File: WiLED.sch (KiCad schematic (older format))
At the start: 23 parts, among them P1 DC In, P2 LED Connector, P3 Serial to USB, P4 ADAFRUIT_FEATHER, SW1 Reset, SW2 Bootload, U1 ESP-12, U2 R-78E-0.5

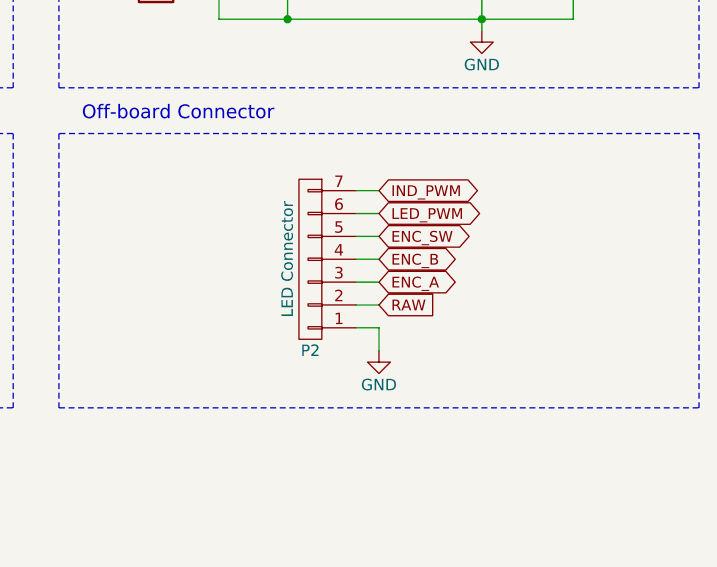
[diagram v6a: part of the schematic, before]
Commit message: Add pull-down on LED_PWM. Closes #1
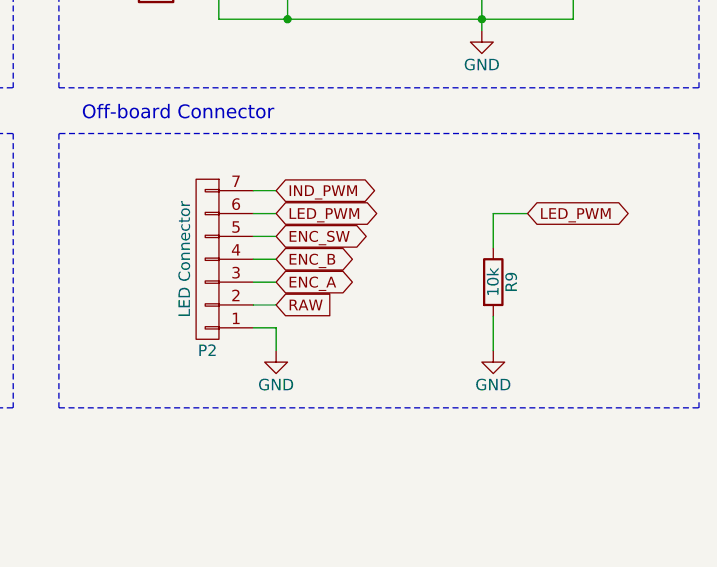
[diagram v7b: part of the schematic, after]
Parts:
- added R9: 10k, Resistors_SMD:R_0805_HandSoldering, symbol R
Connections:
- net GND: now also R9.2
- net LED_PWM: now also R9.1
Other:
- moved on the sheet: P2
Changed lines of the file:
@@
 Sheet 1 1
 Title "WiLED ESP-12 Feather"
-Date "2017-09-10"
-Rev "1.0"
+Date "2017-09-25"
+Rev "1.1"
 Comp "Sean Lanigan"
 Comment1 "Requires RF69 Featherwing to connect to low-power radio network."
@@
 $EndComp
 $Comp
-L GND #PWR01
+L GND #PWR1
 U 1 1 5988430F
 P 2050 1350
-F 0 "#PWR01" H 2050 1100 50  0001 C CNN
+F 0 "#PWR1" H 2050 1100 50  0001 C CNN
 F 1 "GND" H 2050 1200 50  0000 C CNN
 F 2 "" H 2050 1350 50  0000 C CNN
@@
 $EndComp
 $Comp
-L +3.3V #PWR02
+L +3.3V #PWR2
 U 1 1 598859CA
 P 2450 4150
-F 0 "#PWR02" H 2450 4000 50  0001 C CNN
+F 0 "#PWR2" H 2450 4000 50  0001 C CNN
 F 1 "+3.3V" H 2450 4290 50  0000 C CNN
 F 2 "" H 2450 4150 50  0000 C CNN
@@
 $EndComp
 $Comp
-L GND #PWR03
+L GND #PWR3
 U 1 1 59885B82
 P 2450 4900
-F 0 "#PWR03" H 2450 4650 50  0001 C CNN
+F 0 "#PWR3" H 2450 4650 50  0001 C CNN
 F 1 "GND" H 2450 4750 50  0000 C CNN
 F 2 "" H 2450 4900 50  0000 C CNN
@@
 RST
 $Comp
-L +3.3V #PWR04
+L +3.3V #PWR14
 U 1 1 599572FE
 P 8550 1150
-F 0 "#PWR04" H 8550 1000 50  0001 C CNN
+F 0 "#PWR14" H 8550 1000 50  0001 C CNN
 F 1 "+3.3V" H 8550 1290 50  0000 C CNN
 F 2 "" H 8550 1150 50  0000 C CNN
@@
 $EndComp
 $Comp
-L GND #PWR05
+L GND #PWR15
 U 1 1 599575DC
 P 8550 1850
-F 0 "#PWR05" H 8550 1600 50  0001 C CNN
+F 0 "#PWR15" H 8550 1600 50  0001 C CNN
 F 1 "GND" H 8550 1700 50  0000 C CNN
 F 2 "" H 8550 1850 50  0000 C CNN
@@
 EN
 $Comp
-L +3.3V #PWR06
+L +3.3V #PWR16
 U 1 1 59957B8D
 P 9100 1150
-F 0 "#PWR06" H 9100 1000 50  0001 C CNN
+F 0 "#PWR16" H 9100 1000 50  0001 C CNN
 F 1 "+3.3V" H 9100 1290 50  0000 C CNN
 F 2 "" H 9100 1150 50  0000 C CNN
@@
 $EndComp
 $Comp
-L +3.3V #PWR07
+L +3.3V #PWR4
 U 1 1 599586BB
 P 2650 1250
-F 0 "#PWR07" H 2650 1100 50  0001 C CNN
+F 0 "#PWR4" H 2650 1100 50  0001 C CNN
 F 1 "+3.3V" H 2650 1390 50  0000 C CNN
 F 2 "" H 2650 1250 50  0000 C CNN
@@
 LED_PWM
 $Comp
-L GND #PWR08
+L GND #PWR5
 U 1 1 59959BA4
 P 2650 3200
-F 0 "#PWR08" H 2650 2950 50  0001 C CNN
+F 0 "#PWR5" H 2650 2950 50  0001 C CNN
 F 1 "GND" H 2650 3050 50  0000 C CNN
 F 2 "" H 2650 3200 50  0000 C CNN
@@
 2
 $Comp
-L +3.3V #PWR09
+L +3.3V #PWR18
 U 1 1 5995A16C
 P 9650 1150
-F 0 "#PWR09" H 9650 1000 50  0001 C CNN
+F 0 "#PWR18" H 9650 1000 50  0001 C CNN
 F 1 "+3.3V" H 9650 1290 50  0000 C CNN
 F 2 "" H 9650 1150 50  0000 C CNN
@@
 0
 $Comp
-L +3.3V #PWR010
+L +3.3V #PWR21
 U 1 1 5995A6E0
 P 10200 1150
-F 0 "#PWR010" H 10200 1000 50  0001 C CNN
+F 0 "#PWR21" H 10200 1000 50  0001 C CNN
 F 1 "+3.3V" H 10200 1290 50  0000 C CNN
 F 2 "" H 10200 1150 50  0000 C CNN
@@
 $EndComp
 $Comp
-L GND #PWR011
+L GND #PWR22
 U 1 1 5995ABD4
 P 10200 1850
-F 0 "#PWR011" H 10200 1600 50  0001 C CNN
+F 0 "#PWR22" H 10200 1600 50  0001 C CNN
 F 1 "GND" H 10200 1700 50  0000 C CNN
 F 2 "" H 10200 1850 50  0000 C CNN
@@
 15
 $Comp
-L GND #PWR012
+L GND #PWR24
 U 1 1 5995B592
 P 10750 1850
-F 0 "#PWR012" H 10750 1600 50  0001 C CNN
+F 0 "#PWR24" H 10750 1600 50  0001 C CNN
 F 1 "GND" H 10750 1700 50  0000 C CNN
 F 2 "" H 10750 1850 50  0000 C CNN
@@
 $EndComp
 $Comp
-L GND #PWR013
+L GND #PWR19
 U 1 1 5996B043
 P 10000 3250
-F 0 "#PWR013" H 10000 3000 50  0001 C CNN
+F 0 "#PWR19" H 10000 3000 50  0001 C CNN
 F 1 "GND" H 10000 3100 50  0000 C CNN
 F 2 "" H 10000 3250 50  0000 C CNN
@@
 $EndComp
 $Comp
-L +3.3V #PWR014
+L +3.3V #PWR23
 U 1 1 5996BEF5
 P 10500 2600
-F 0 "#PWR014" H 10500 2450 50  0001 C CNN
+F 0 "#PWR23" H 10500 2450 50  0001 C CNN
 F 1 "+3.3V" H 10500 2740 50  0000 C CNN
 F 2 "" H 10500 2600 50  0000 C CNN
@@
 Text GLabel 3550 4700 0    47   Input ~ 0
 RAW
-Text GLabel 9550 4450 2    47   Input ~ 0
+Text GLabel 9100 4450 2    47   Input ~ 0
 RAW
 $Comp
-L GND #PWR015
+L GND #PWR17
 U 1 1 5997B5E9
-P 9550 4650
-F 0 "#PWR015" H 9550 4400 50  0001 C CNN
-F 1 "GND" H 9550 4500 50  0000 C CNN
-F 2 "" H 9550 4650 50  0000 C CNN
-F 3 "" H 9550 4650 50  0000 C CNN
-	1    9550 4650
-	1    0    0    -1
-$EndComp
-Text GLabel 9550 4050 2    47   BiDi ~ 0
+P 9100 4650
+F 0 "#PWR17" H 9100 4400 50  0001 C CNN
+F 1 "GND" H 9100 4500 50  0000 C CNN
+F 2 "" H 9100 4650 50  0000 C CNN
+F 3 "" H 9100 4650 50  0000 C CNN
+	1    9100 4650
+	1    0    0    -1
+$EndComp
+Text GLabel 9100 4050 2    47   BiDi ~ 0
 LED_PWM
 Text GLabel 3800 2350 2    47   BiDi ~ 0
@@
 Text GLabel 3800 2550 2    47   BiDi ~ 0
 ENC_B
-Text GLabel 9550 4350 2    47   BiDi ~ 0
+Text GLabel 9100 4350 2    47   BiDi ~ 0
 ENC_A
-Text GLabel 9550 4250 2    47   BiDi ~ 0
+Text GLabel 9100 4250 2    47   BiDi ~ 0
 ENC_B
-Text GLabel 9550 4150 2    47   BiDi ~ 0
+Text GLabel 9100 4150 2    47   BiDi ~ 0
 ENC_SW
-Text GLabel 9550 3950 2    47   BiDi ~ 0
+Text GLabel 9100 3950 2    47   BiDi ~ 0
 IND_PWM
 Text Notes 8250 3650 0    60   ~ 0
@@
 $EndComp
 $Comp
-L GND #PWR016
+L GND #PWR10
 U 1 1 59982D30
 P 6550 4350
-F 0 "#PWR016" H 6550 4100 50  0001 C CNN
+F 0 "#PWR10" H 6550 4100 50  0001 C CNN
 F 1 "GND" H 6550 4200 50  0000 C CNN
 F 2 "" H 6550 4350 50  0000 C CNN
@@
 $EndComp
 $Comp
-L GND #PWR017
+L GND #PWR13
 U 1 1 5998304D
 P 7400 4350
-F 0 "#PWR017" H 7400 4100 50  0001 C CNN
+F 0 "#PWR13" H 7400 4100 50  0001 C CNN
 F 1 "GND" H 7400 4200 50  0000 C CNN
 F 2 "" H 7400 4350 50  0000 C CNN
@@
 $EndComp
 $Comp
-L GND #PWR018
+L GND #PWR11
 U 1 1 5999AA51
 P 6650 1800
-F 0 "#PWR018" H 6650 1550 50  0001 C CNN
+F 0 "#PWR11" H 6650 1550 50  0001 C CNN
 F 1 "GND" H 6650 1650 50  0000 C CNN
 F 2 "" H 6650 1800 50  0000 C CNN
@@
 Power LED
 $Comp
-L +3.3V #PWR019
+L +3.3V #PWR9
 U 1 1 59B07E62
 P 5800 2800
-F 0 "#PWR019" H 5800 2650 50  0001 C CNN
+F 0 "#PWR9" H 5800 2650 50  0001 C CNN
 F 1 "+3.3V" H 5800 2940 50  0000 C CNN
 F 2 "" H 5800 2800 50  0000 C CNN
@@
 $EndComp
 $Comp
-L GND #PWR020
+L GND #PWR12
 U 1 1 59B08869
 P 7200 3050
-F 0 "#PWR020" H 7200 2800 50  0001 C CNN
+F 0 "#PWR12" H 7200 2800 50  0001 C CNN
 F 1 "GND" H 7200 2900 50  0000 C CNN
 F 2 "" H 7200 3050 50  0000 C CNN
@@
 ENC_SW
 $Comp
-L +3.3V #PWR021
+L +3.3V #PWR7
 U 1 1 59B0DF7F
 P 5750 3900
-F 0 "#PWR021" H 5750 3750 50  0001 C CNN
+F 0 "#PWR7" H 5750 3750 50  0001 C CNN
 F 1 "+3.3V" H 5750 4040 50  0000 C CNN
 F 2 "" H 5750 3900 50  0000 C CNN
@@
 $EndComp
 $Comp
-L GND #PWR022
+L GND #PWR8
 U 1 1 59B10828
 P 5750 4700
-F 0 "#PWR022" H 5750 4450 50  0001 C CNN
+F 0 "#PWR8" H 5750 4450 50  0001 C CNN
 F 1 "GND" H 5750 4550 50  0000 C CNN
 F 2 "" H 5750 4700 50  0000 C CNN
@@
 	5150 900  5150 2100
 $Comp
-L GND #PWR023
+L GND #PWR6
 U 1 1 59B4D73F
 P 3000 5500
-F 0 "#PWR023" H 3000 5250 50  0001 C CNN
+F 0 "#PWR6" H 3000 5250 50  0001 C CNN
 F 1 "GND" H 3000 5350 50  0000 C CNN
 F 2 "" H 3000 5500 50  0000 C CNN
@@
 L CONN_01X07 P2
 U 1 1 59B5296F
-P 9250 4250
-F 0 "P2" H 9250 4650 50  0000 C CNN
-F 1 "LED Connector" V 9350 4250 50  0000 C CNN
-F 2 "Connectors_JST:JST_PH_B7B-PH-K_07x2.00mm_Straight" H 9250 4250 50  0001 C CNN
-F 3 "" H 9250 4250 50  0000 C CNN
-	1    9250 4250
+P 8800 4250
+F 0 "P2" H 8800 4650 50  0000 C CNN
+F 1 "LED Connector" V 8900 4250 50  0000 C CNN
+F 2 "Connectors_JST:JST_PH_B7B-PH-K_07x2.00mm_Straight" H 8800 4250 50  0001 C CNN
+F 3 "" H 8800 4250 50  0000 C CNN
+	1    8800 4250
 	-1   0    0    1
 $EndComp
 Wire Wire Line
-	9450 4550 9550 4550
-Wire Wire Line
-	9550 4550 9550 4650
-Wire Wire Line
-	9450 3950 9550 3950
-Wire Wire Line
-	9450 4050 9550 4050
-Wire Wire Line
-	9450 4150 9550 4150
-Wire Wire Line
-	9450 4250 9550 4250
-Wire Wire Line
-	9450 4350 9550 4350
-Wire Wire Line
-	9450 4450 9550 4450
+	9000 4550 9100 4550
+Wire Wire Line
+	9100 4550 9100 4650
+Wire Wire Line
+	9000 3950 9100 3950
+Wire Wire Line
+	9000 4050 9100 4050
+Wire Wire Line
+	9000 4150 9100 4150
+Wire Wire Line
+	9000 4250 9100 4250
+Wire Wire Line
+	9000 4350 9100 4350
+Wire Wire Line
+	9000 4450 9100 4450
 NoConn ~ 2000 5800
+Text GLabel 10200 4050 2    47   BiDi ~ 0
+LED_PWM
+$Comp
+L R R9
+U 1 1 59C8F140
+P 10050 4350
+F 0 "R9" V 10130 4350 50  0000 C CNN
+F 1 "10k" V 10050 4350 50  0000 C CNN
+F 2 "Resistors_SMD:R_0805_HandSoldering" V 9980 4350 50  0001 C CNN
+F 3 "" H 10050 4350 50  0000 C CNN
+	1    10050 4350
+	1    0    0    -1
+$EndComp
+$Comp
+L GND #PWR20
+U 1 1 59C8F1EB
+P 10050 4650
+F 0 "#PWR20" H 10050 4400 50  0001 C CNN
+F 1 "GND" H 10050 4500 50  0000 C CNN
+F 2 "" H 10050 4650 50  0000 C CNN
+F 3 "" H 10050 4650 50  0000 C CNN
+	1    10050 4650
+	1    0    0    -1
+$EndComp
+Wire Wire Line
+	10200 4050 10050 4050
+Wire Wire Line
+	10050 4050 10050 4200
+Wire Wire Line
+	10050 4500 10050 4650
 $EndSCHEMATC

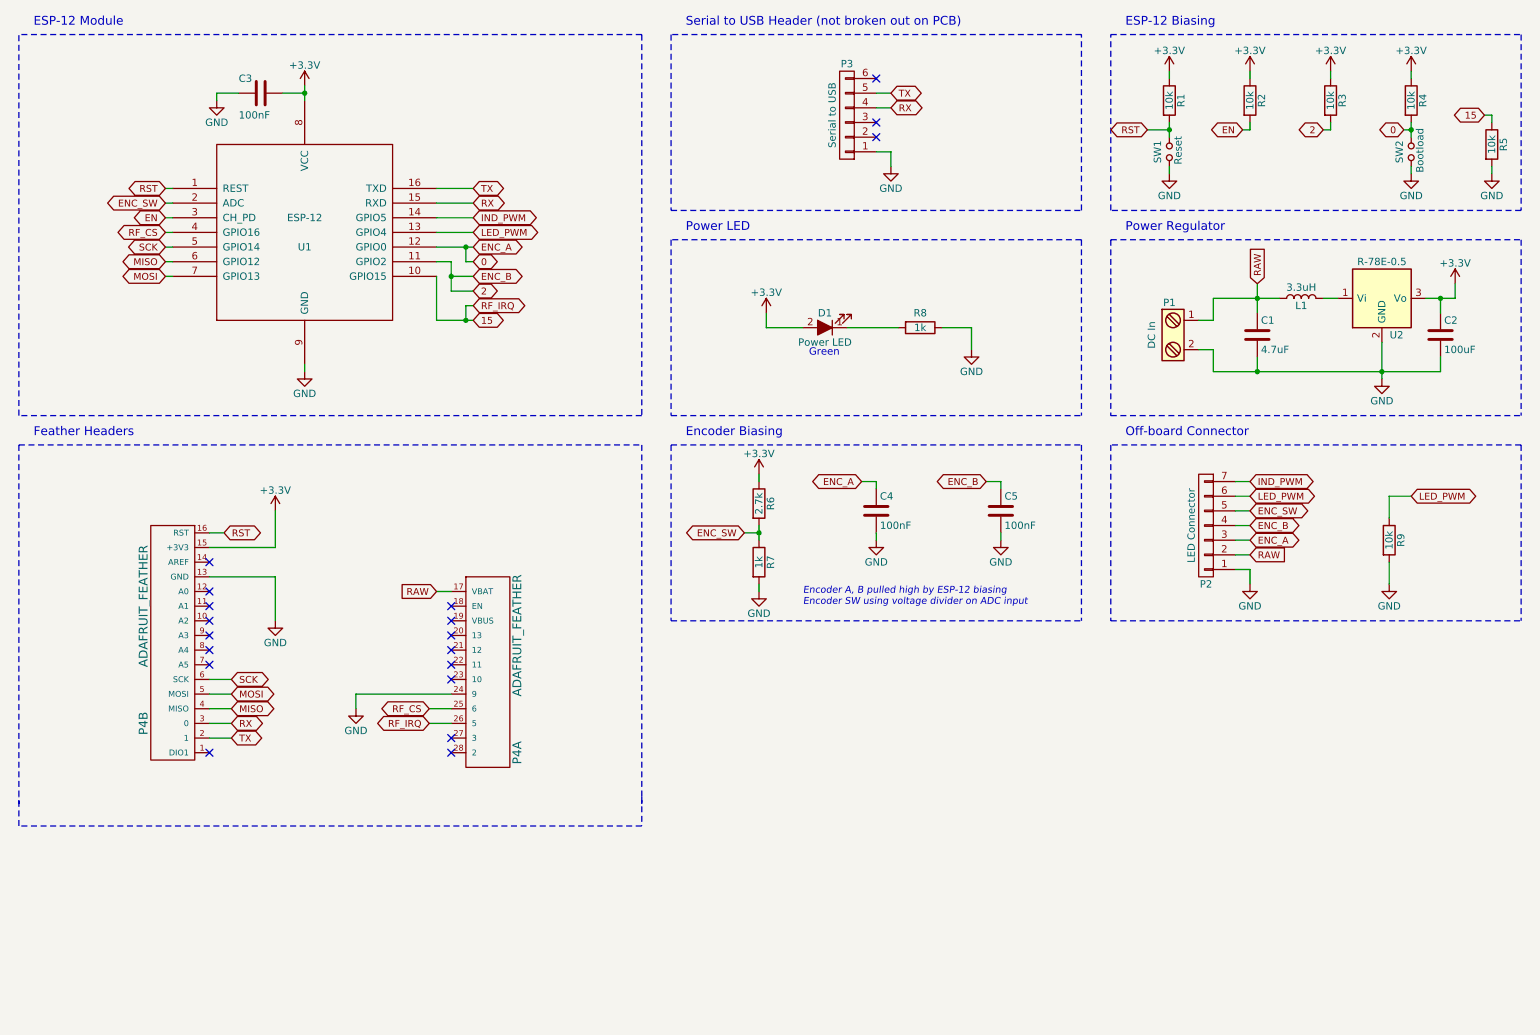
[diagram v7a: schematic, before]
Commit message: Update schematic to Version 2.0, using the ESP-WROOM-32
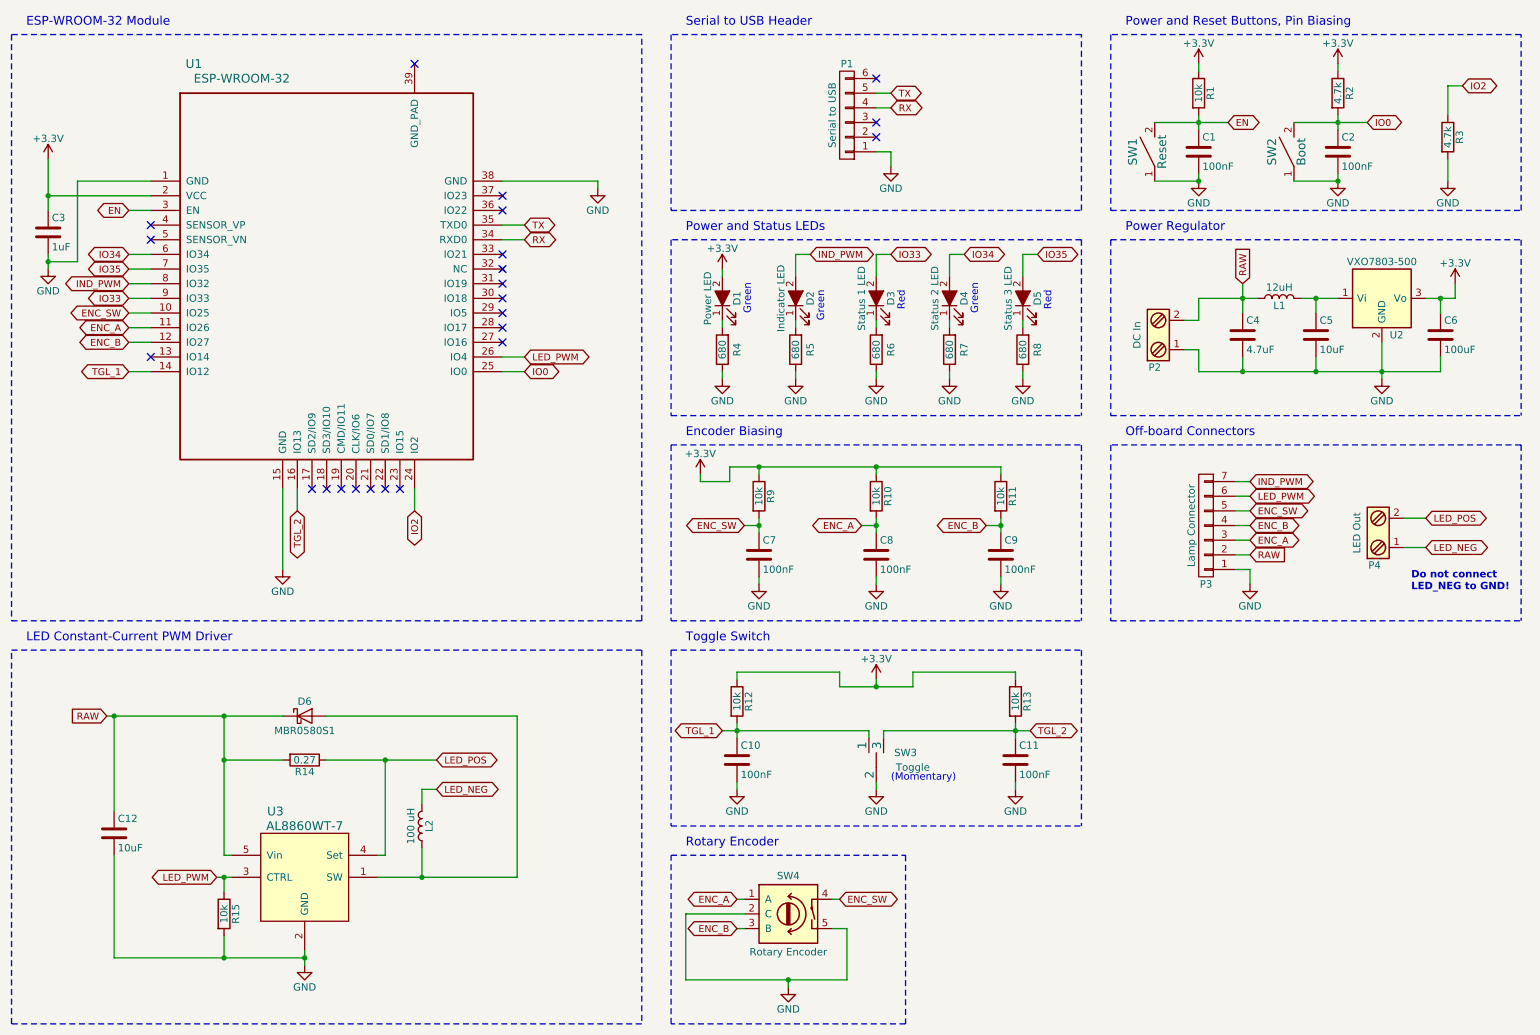
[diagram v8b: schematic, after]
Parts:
- removed P2: LED Connector, Connectors_JST:JST_PH_B7B-PH-K_07x2.00mm_Straight, symbol CONN_01X07
- removed P4: ADAFRUIT_FEATHER, custom-footprints:ADAFRUIT_FEATHER, symbol ADAFRUIT_FEATHER
- removed R4: 10k, Resistors_SMD:R_0805_HandSoldering, symbol R
- removed SW1: Reset, custom-footprints:Button_6.5mm, symbol Jumper_NO_Small
- removed SW2: Bootload, Socket_Strips:Socket_Strip_Straight_1x02, symbol Jumper_NO_Small
- removed U1: ESP-12, custom-footprints:ESP-12E_compact, symbol ESP-12
- added C1, C10, C11, C2, C7: 100nF, Capacitors_SMD:C_0805_HandSoldering, symbol C
- added C12, C5: 10uF, Capacitors_SMD:C_0805_HandSoldering, symbol C
- added D2: Indicator LED, LEDs:LED-3MM, symbol LED_ALT
- added D3: Status 1 LED, LEDs:LED-3MM, symbol LED_ALT
- added D4: Status 2 LED, LEDs:LED-3MM, symbol LED_ALT
- added D5: Status 3 LED, LEDs:LED-3MM, symbol LED_ALT
- added D6: MBR0580S1, symbol D_Schottky
- added L2: 100 uH, custom-footprints:THT_Inductor_small, symbol L
- added P3: Lamp Connector, Connectors_JST:JST_PH_B7B-PH-K_07x2.00mm_Straight, symbol CONN_01X07
- added P4: LED Out, Connectors_JST:JST_PH_B2B-PH-K_02x2.00mm_Straight, symbol Screw_Terminal_1x02
- added R10, R11, R12, R13, R15: 10k, Resistors_SMD:R_0805_HandSoldering, symbol R
- added R14: 0.27, Resistors_SMD:R_0805_HandSoldering, symbol R
- added R8: 680, Resistors_SMD:R_0805_HandSoldering, symbol R
- added SW1: Reset, symbol SWITCH_SPST
- added SW2: Boot, symbol SWITCH_SPST
- added SW3: Toggle, symbol SWITCH_SPDT
- added SW4: Rotary Encoder, symbol Rotary_Encoder_Switch
- added U1: ESP-WROOM-32, ESP32-footprints-Lib:ESP32-WROOM, symbol ESP32-WROOM
- added U3: AL8860WT-7, symbol AL8860WT-7
- C3: value 100nF -> 1uF
- L1: value 3.3uH -> 12uH
- R2, R3: value 10k -> 4.7k
- R4: renamed from R8; value 1k -> 680
- R5: value 10k -> 680
- R6: value 2.7k -> 680
- R7: value 1k -> 680
- U2: value R-78E-0.5 -> VXO7803-500
- renumbered C1 to C4, C2 to C6, C4 to C8, C5 to C9, P3 to P1, P1 to P2
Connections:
- net 15 is gone; now on net GND: R5.1
- net RST is gone; now on net EN: R1.2
- net +3V3: now also R9.1, R10.1, R11.1, R12.1, R13.1, U1.2 (VCC); no longer R3.1, R6.1
- net EN: now also C1.1, SW1.2, U1.3 (EN); no longer R2.2
- net ENC_SW: now also R9.2, C7.1, P3.5 (P5), SW4.4, U1.10 (IO25); no longer R6.2, R7.1
- net GND: now also P2.1, R3.2, R6.1, R7.1, C1.2, C10.2, C11.2, C12.2, C2.2, C5.2, C7.2, P3.1 (P1), R15.2, R8.1, SW1.1, SW2.1, SW3.2, SW4.2 (C), SW4.5, U1.1 (GND), U1.15 (GND), U1.38 (GND), U3.2 (GND); no longer P2.2, R5.2, R7.2, R9.2
- net IND_PWM: now also D2.2 (A), P3.7 (P7), U1.8 (IO32)
- net LED_PWM: now also P3.6 (P6), R15.1, U1.26 (IO4), U3.3 (CTRL); no longer R9.1
- net RAW: now also P2.2, C12.1, D6.1 (K), P3.2 (P2), R14.2, U3.5 (Vin); no longer P2.1
- net RX: now also U1.34 (RXD0)
- net TX: now also U1.35 (TXD0)
- net at L1.2, U2.1 (Vi): now also C5.1
- net 0 renamed ENC_A
- net ENC_A: now also P3.3 (P3), R10.2, SW4.1 (A), U1.11 (IO26)
- net 2 renamed ENC_B
- net ENC_B: now also P3.4 (P4), R11.2, SW4.3 (B), U1.12 (IO27); no longer R3.2
- new net: D3.1 (K), R6.2
- new net: D4.1 (K), R7.2
- new net: D5.1 (K), R8.2
- new net: D6.2 (A), L2.1, U3.1 (SW)
- new net: D2.1 (K), R5.2
- new net IO0: C2.1, R2.2, SW2.2, U1.25 (IO0)
- new net IO2: R3.1, U1.24 (IO2)
- new net IO33: D3.2 (A), U1.9 (IO33)
- new net IO34: D4.2 (A), U1.6 (IO34)
- new net IO35: D5.2 (A), U1.7 (IO35)
- new net LED_NEG: L2.2, P4.1
- new net LED_POS: P4.2, R14.1, U3.4 (Set)
- new net TGL_1: C10.1, R12.2, SW3.1, U1.14 (IO12)
- new net TGL_2: C11.1, R13.2, SW3.3, U1.16 (IO13)
- no-connect marks 19 -> 23
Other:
- note added: "(Momentary)"
- note added: "Do not connect \nLED_NEG to GND!"
- note added: "ESP-WROOM-32 Module"
- note added: "LED Constant-Current PWM Driver"
- note added: "Off-board Connectors"
- note added: "Power and Reset Buttons, Pin Biasing"
- note added: "Power and Status LEDs"
- note added: "Red"
- note added: "Rotary Encoder"
- note added: "Serial to USB Header"
- note added: "Toggle Switch"
- note removed: "ESP-12 Biasing"
- note removed: "ESP-12 Module"
- note removed: "Encoder A, B pulled high by ESP-12 biasing\nEncoder SW using voltage divider on ADC input"
- note removed: "Feather Headers"
- note removed: "Off-board Connector"
- note removed: "Power LED"
- note removed: "Serial to USB Header (not broken out on PCB)"
- moved on the sheet: C4, C8, C9, D1, L1, P2, R4
